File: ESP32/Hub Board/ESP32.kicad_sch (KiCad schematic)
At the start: 23 parts, among them Q1 SS8050-G, Q2 SS8050-G, SW1 SW_Push, SW2 SW_Push, U2 ESP32-S3-WROOM-1-N16R2

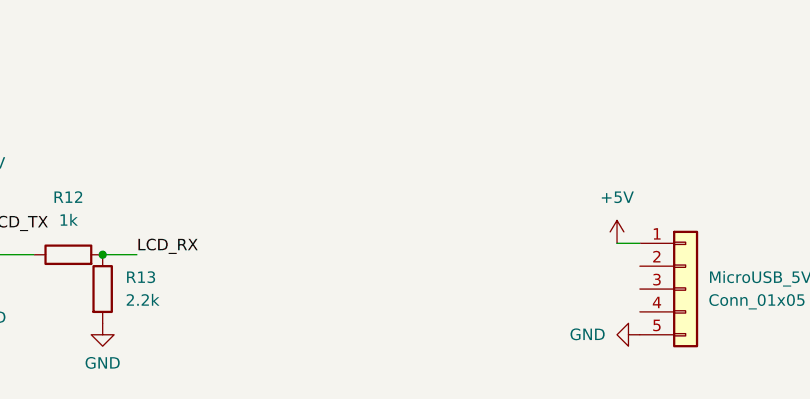
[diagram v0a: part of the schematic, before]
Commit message: Added voltage regulators to both schematics
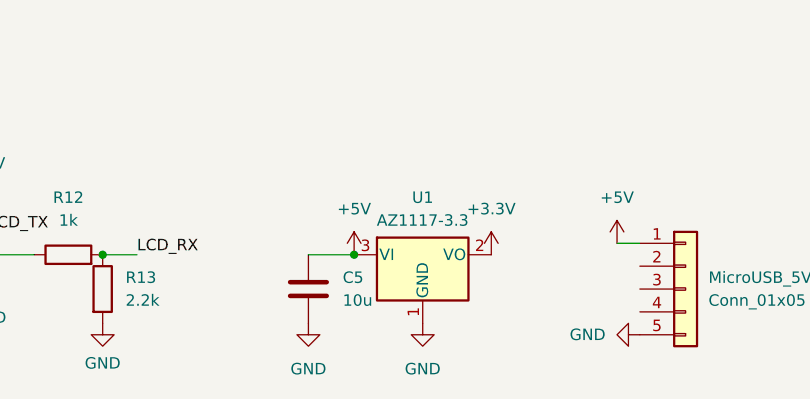
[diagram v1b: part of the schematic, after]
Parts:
- added C5: 10u, symbol Device:C
- added U1: AZ1117-3.3, symbol Regulator_Linear:AZ1117-3.3
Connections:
- net +5V: now also C5.1, U1.3 (VI)
- net GND: now also C5.2, U1.1 (GND)
- new net +3.3V: U1.2 (VO)
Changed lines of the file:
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@@
   (junction (at 245.745 59.69) (diameter 0) (color 0 0 0 0)
   )
+  (junction (at 217.17 140.97) (diameter 0) (color 0 0 0 0)
+  )
   (junction (at 245.745 57.15) (diameter 0) (color 0 0 0 0)
   )
@@
   )
   (wire (pts (xy 50.8 40.64) (xy 50.8 43.18))
+    (stroke (width 0) (type default))
+  )
+  (wire (pts (xy 212.09 140.97) (xy 217.17 140.97))
     (stroke (width 0) (type default))
   )
@@
     )
   )
+  (symbol (lib_id "power:+3.3V") (at 232.41 140.97 0) (unit 1)
+    (in_bom yes) (on_board yes) (dnp no) (fields_autoplaced)
+    (property "Reference" "#PWR015" (at 232.41 144.78 0)
+      (effects (font (size 1.27 1.27)) hide)
+    )
+    (property "Value" "+3.3V" (at 232.41 135.89 0)
+      (effects (font (size 1.27 1.27)))
+    )
+    (property "Footprint" "" (at 232.41 140.97 0)
+      (effects (font (size 1.27 1.27)) hide)
+    )
+    (property "Datasheet" "" (at 232.41 140.97 0)
+      (effects (font (size 1.27 1.27)) hide)
+    )
+    (pin "1")
+    (instances
+      (project "ESP32"
+        (path "/668738a4-4fba-4c81-8219-00fa4ae32623"
+          (reference "#PWR015") (unit 1)
+        )
+      )
+    )
+  )
   (symbol (lib_id "power:+5V") (at 176.53 135.89 0) (unit 1)
     (in_bom yes) (on_board yes) (dnp no) (fields_autoplaced)
@@
     )
   )
+  (symbol (lib_name "GND_2") (lib_id "power:GND") (at 212.09 148.59 0) (unit 1)
+    (in_bom yes) (on_board yes) (dnp no) (fields_autoplaced)
+    (property "Reference" "#PWR012" (at 212.09 154.94 0)
+      (effects (font (size 1.27 1.27)) hide)
+    )
+    (property "Value" "GND" (at 212.09 153.67 0)
+      (effects (font (size 1.27 1.27)))
+    )
+    (property "Footprint" "" (at 212.09 148.59 0)
+      (effects (font (size 1.27 1.27)) hide)
+    )
+    (property "Datasheet" "" (at 212.09 148.59 0)
+      (effects (font (size 1.27 1.27)) hide)
+    )
+    (pin "1")
+    (instances
+      (project "ESP32"
+        (path "/668738a4-4fba-4c81-8219-00fa4ae32623"
+          (reference "#PWR012") (unit 1)
+        )
+      )
+    )
+  )
   (symbol (lib_id "power:+5V") (at 246.38 139.7 0) (unit 1)
     (in_bom yes) (on_board yes) (dnp no) (fields_autoplaced)
@@
         (path "/668738a4-4fba-4c81-8219-00fa4ae32623"
           (reference "#PWR023") (unit 1)
+        )
+      )
+    )
+  )
+  (symbol (lib_id "Device:C") (at 212.09 144.78 0) (unit 1)
+    (in_bom yes) (on_board yes) (dnp no) (fields_autoplaced)
+    (property "Reference" "C5" (at 215.9 143.51 0)
+      (effects (font (size 1.27 1.27)) (justify left))
+    )
+    (property "Value" "10u" (at 215.9 146.05 0)
+      (effects (font (size 1.27 1.27)) (justify left))
+    )
+    (property "Footprint" "" (at 213.0552 148.59 0)
+      (effects (font (size 1.27 1.27)) hide)
+    )
+    (property "Datasheet" "~" (at 212.09 144.78 0)
+      (effects (font (size 1.27 1.27)) hide)
+    )
+    (pin "2")
+    (pin "1")
+    (instances
+      (project "ESP32"
+        (path "/668738a4-4fba-4c81-8219-00fa4ae32623"
+          (reference "C5") (unit 1)
         )
       )
@@
     )
   )
+  (symbol (lib_name "GND_1") (lib_id "power:GND") (at 224.79 148.59 0) (unit 1)
+    (in_bom yes) (on_board yes) (dnp no) (fields_autoplaced)
+    (property "Reference" "#PWR014" (at 224.79 154.94 0)
+      (effects (font (size 1.27 1.27)) hide)
+    )
+    (property "Value" "GND" (at 224.79 153.67 0)
+      (effects (font (size 1.27 1.27)))
+    )
+    (property "Footprint" "" (at 224.79 148.59 0)
+      (effects (font (size 1.27 1.27)) hide)
+    )
+    (property "Datasheet" "" (at 224.79 148.59 0)
+      (effects (font (size 1.27 1.27)) hide)
+    )
+    (pin "1")
+    (instances
+      (project "ESP32"
+        (path "/668738a4-4fba-4c81-8219-00fa4ae32623"
+          (reference "#PWR014") (unit 1)
+        )
+      )
+    )
+  )
   (symbol (lib_id "basic:R") (at 71.12 93.98 90) (unit 1)
     (in_bom yes) (on_board yes) (dnp no) (fields_autoplaced)
@@
     )
   )
+  (symbol (lib_id "Regulator_Linear:AZ1117-3.3") (at 224.79 140.97 0) (unit 1)
+    (in_bom yes) (on_board yes) (dnp no) (fields_autoplaced)
+    (property "Reference" "U1" (at 224.79 134.62 0)
+      (effects (font (size 1.27 1.27)))
+    )
+    (property "Value" "AZ1117-3.3" (at 224.79 137.16 0)
+      (effects (font (size 1.27 1.27)))
+    )
+    (property "Footprint" "" (at 224.79 134.62 0)
+      (effects (font (size 1.27 1.27) italic) hide)
+    )
+    (property "Datasheet" "https://www.diodes.com/assets/Datasheets/AZ1117.pdf" (at 224.79 140.97 0)
+      (effects (font (size 1.27 1.27)) hide)
+    )
+    (pin "1")
+    (pin "3")
+    (pin "2")
+    (instances
+      (project "ESP32"
+        (path "/668738a4-4fba-4c81-8219-00fa4ae32623"
+          (reference "U1") (unit 1)
+        )
+      )
+    )
+  )
   (symbol (lib_id "power:+3V3") (at 147.32 31.75 0) (unit 1)
     (in_bom yes) (on_board yes) (dnp no) (fields_autoplaced)
@@
         )
       )
+    )
+  )
+  (symbol (lib_id "power:+5V") (at 217.17 140.97 0) (unit 1)
+    (in_bom yes) (on_board yes) (dnp no) (fields_autoplaced)
+    (property "Reference" "#PWR013" (at 217.17 144.78 0)
+      (effects (font (size 1.27 1.27)) hide)
+    )
+    (property "Value" "+5V" (at 217.17 135.89 0)
+      (effects (font (size 1.27 1.27)))
+    )
+    (property "Footprint" "" (at 217.17 140.97 0)
+      (effects (font (size 1.27 1.27)) hide)
+    )
+    (property "Datasheet" "" (at 217.17 140.97 0)
+      (effects (font (size 1.27 1.27)) hide)
+    )
+    (pin "1")
+    (instances
+      (project "ESP32"
+        (path "/668738a4-4fba-4c81-8219-00fa4ae32623"
+          (reference "#PWR013") (unit 1)
+        )
+      )
